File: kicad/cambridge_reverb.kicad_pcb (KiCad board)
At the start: 2 copper layers, 190 x 115 mm, 144 parts, among them IC1 TL072CP, IC2 TL072CP, Q1 MMBF5457, Q2 MMBF5457, T1 reuse / AnTek AS-0524, U1 LM317T

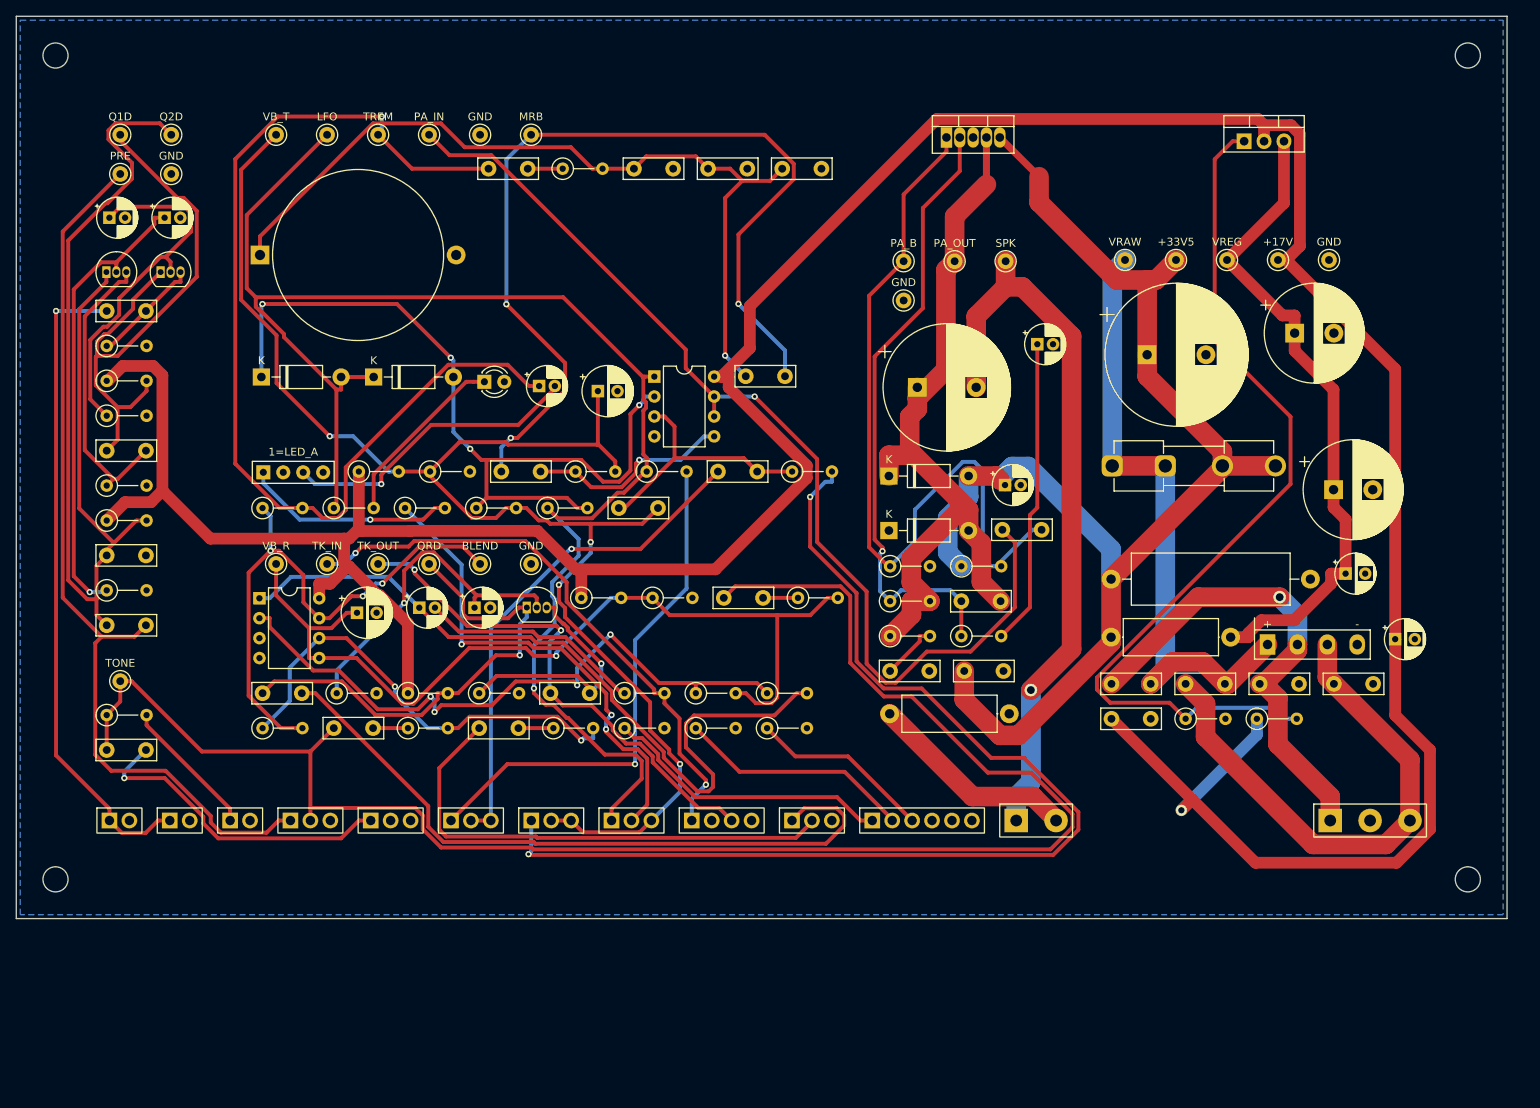
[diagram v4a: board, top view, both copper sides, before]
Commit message: Tone stack: Bass + Treble (passive James) with a switchable mid cut (errata #20)
The panel has Bass and Treble pots, but the design carried a single treble-cut
"Tone" substitute -- and the recovered preamp coupling was the 470 pF chime cap
alone, a 1.3 kHz high-pass that passed no bass at all. Replace both:

- C_cpl_out 1 uF full-band coupling from Q2's drain; C_treble 470 pF becomes a
  bright cap across the top of the volume pot.
- Passive James (Thomas-Vox) Bass/Treble network -- the originals' topology,
  asymmetric, more cut than boost, kept over an active Baxandall so the amp
  keeps its character -- driven by a TL074 (IC3: input buffer, x2 make-up,
  gyrator, output buffer) on its own mid-rail VBIAS_3. Both pots 250k lin in
  the original holes.
- MID CUT toggle for honky pickups: R_mid + a switched series-resonant gyrator
  shunt (1.86 H simulated + 22 nF): -9.6 dB at ~800 Hz, Q ~0.6, flat when off,
  no DC across the switch. SW_MID sits in the original line-reverse switch
  hole -- no new panel holes.
- SPICE: ac_tonestack.cir rewritten rail-aware (all IC3 nodes 8.50 V, noon
  -0.21 dB, notch -9.65 dB at 796 Hz); sweep_tonestack.cir sweeps both pots
  and the switch; results committed.

Generator / placer / router:
- OPAMP14 and SW_SPST symbols, VB_3 / TMK test points (28), BOM rows for IC3,
  the DIP-14 socket, POT_BASS/POT_TREB, SW_MID.
- gen_pcb: tighter profiles (THT 1.2 mm gap / 3.5 mm channels, SMD 0.4 mm),
  overflow repair by moving width between columns, small parts kept in
  schematic order on the shelves, tone/preamp column weighted wider, TP cells
  6x4.5 with the courtyard flush to the cell, input-jack pads down the LEFT
  edge on the 155x90 board (the bottom edge is ~9 mm short for 13 groups),
  keepout rule areas (2 mm edge frame + M3 hole squares) exported to the
  router.
- route_board: refuse a board without its .kicad_pro (a copy routed away from
  the project came back with 0.2 mm tracks and 400 DRC errors); prune
  zero-length segments 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
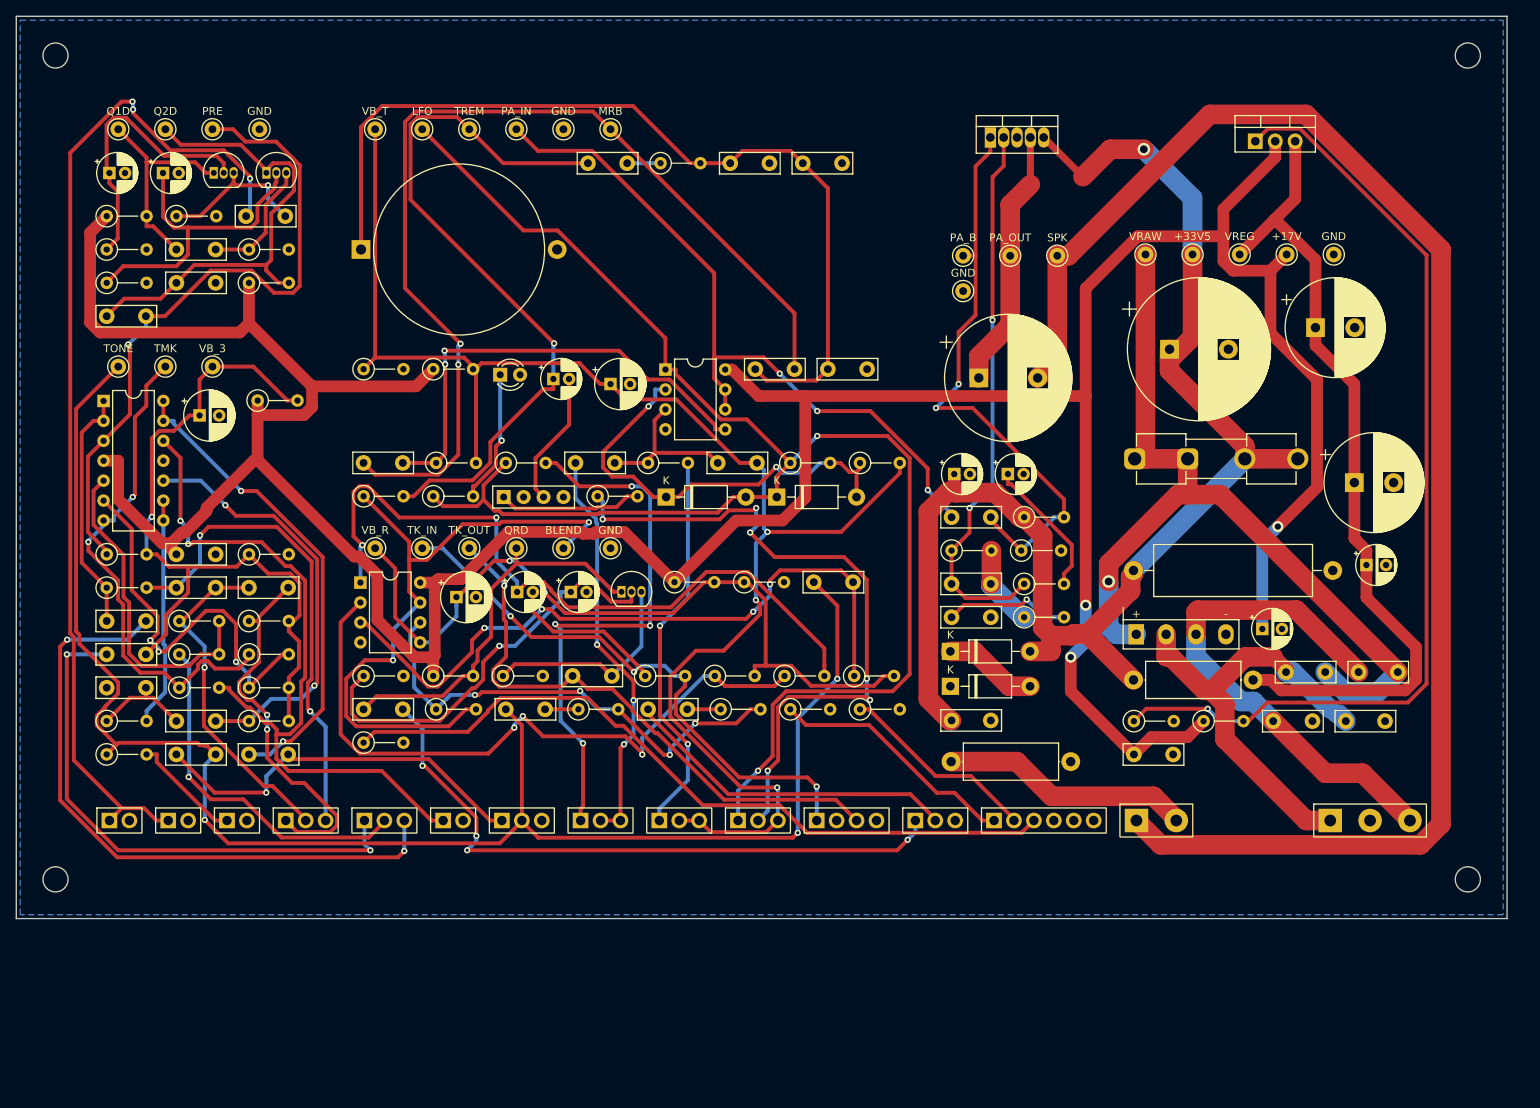
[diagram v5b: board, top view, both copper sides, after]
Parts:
- removed C_cut: 10nF, C_Disc_D7.5mm_W2.5mm_P5.00mm
- removed POT_TONE: 100k lin, WirePad_1x03_P2.54mm_D1.2mm
- added C_byp3: 100nF, C_Disc_D7.5mm_W2.5mm_P5.00mm, F.Cu at (20.4, 68.6)
- added C_cpl_out: 1uF, C_Disc_D7.5mm_W2.5mm_P5.00mm, F.Cu at (11.5, 38.2)
- added C_gg: 1.8nF, C_Disc_D7.5mm_W2.5mm_P5.00mm, F.Cu at (20.4, 89.8)
- added C_j1: 22nF, C_Disc_D7.5mm_W2.5mm_P5.00mm, F.Cu at (20.4, 72.8)
- added C_j2: 22nF, C_Disc_D7.5mm_W2.5mm_P5.00mm, F.Cu at (29.7, 72.8)
- added C_j3: 2.2nF, C_Disc_D7.5mm_W2.5mm_P5.00mm, F.Cu at (11.5, 77.1)
- added C_j4: 2.2nF, C_Disc_D7.5mm_W2.5mm_P5.00mm, F.Cu at (11.5, 81.3)
- added C_res: 22nF, C_Disc_D7.5mm_W2.5mm_P5.00mm, F.Cu at (11.5, 85.6)
- added C_tout: 1uF, C_Disc_D7.5mm_W2.5mm_P5.00mm, F.Cu at (29.7, 94.1)
- added C_vb3: 47uF/25V, CP_Radial_D6.3mm_P2.50mm, F.Cu at (23.4, 50.9)
- added IC3: TL074CN, DIP-14_W7.62mm, F.Cu at (11.1, 49.0)
- added POT_BASS: 250k lin, WirePad_1x03_P2.54mm_D1.2mm, F.Cu at (34.3, 102.5)
- added POT_TREB: 250k lin, WirePad_1x03_P2.54mm_D1.2mm, F.Cu at (44.4, 102.5)
- added R_gL: 4.7k, R_Axial_DIN0207_L6.3mm_D2.5mm_P5.08mm_Vertical, F.Cu at (11.5, 89.8)
- added R_gg: 220k, R_Axial_DIN0207_L6.3mm_D2.5mm_P5.08mm_Vertical, F.Cu at (29.7, 89.8)
- added R_inb: 1M, R_Axial_DIN0207_L6.3mm_D2.5mm_P5.08mm_Vertical, F.Cu at (11.5, 68.6)
- added R_j1: 10k, R_Axial_DIN0207_L6.3mm_D2.5mm_P5.08mm_Vertical, F.Cu at (11.5, 72.8)
- added R_j2: 10k, R_Axial_DIN0207_L6.3mm_D2.5mm_P5.08mm_Vertical, F.Cu at (29.7, 77.1)
- added R_j3: 68k, R_Axial_DIN0207_L6.3mm_D2.5mm_P5.08mm_Vertical, F.Cu at (20.8, 77.1)
- added R_j4: 1k, R_Axial_DIN0207_L6.3mm_D2.5mm_P5.08mm_Vertical, F.Cu at (20.8, 81.3)
- added R_mid: 10k, R_Axial_DIN0207_L6.3mm_D2.5mm_P5.08mm_Vertical, F.Cu at (20.8, 85.6)
- added R_mk1: 10k, R_Axial_DIN0207_L6.3mm_D2.5mm_P5.08mm_Vertical, F.Cu at (29.7, 81.3)
- added R_mk2: 10k, R_Axial_DIN0207_L6.3mm_D2.5mm_P5.08mm_Vertical, F.Cu at (29.7, 85.6)
- added R_vb31: 100k, R_Axial_DIN0207_L6.3mm_D2.5mm_P5.08mm_Vertical, F.Cu at (30.8, 49.0)
- added R_vb32: 100k, R_Axial_DIN0207_L6.3mm_D2.5mm_P5.08mm_Vertical, F.Cu at (29.7, 68.6)
- added SW_MID: MID CUT, WirePad_1x02_P2.54mm_D1.2mm, F.Cu at (54.4, 102.5)
- added TP_MK_OUT: TMK, TestPoint_THT_D2.0mm_Label, F.Cu at (19.0, 44.6)
- added TP_VBIAS_3: VB_3, TestPoint_THT_D2.0mm_Label, F.Cu at (25.0, 44.6)
- moved D_lfo2 53.8 mm to (82.8, 61.3)
- moved D_lfo1 53.6 mm to (96.9, 61.3)
- moved R_fs_mrb 51.5 mm to (44.3, 92.6)
- moved R_lfo_fb2 49.2 mm to (107.5, 56.9)
- moved TP_TONE_OUT 40.1 mm to (13.0, 44.6)
- moved R_s2 39.2 mm to (11.5, 34.0)
- moved C_pres 35.9 mm to (20.4, 34.0)
- moved R_d2 35.3 mm to (29.7, 34.0)
- moved R_g2 35.1 mm to (29.7, 29.7)
- moved R_lfo_fb1 31.5 mm to (98.7, 56.9)
- moved VTL1 30.8 mm to (62.1, 61.3)
- moved C_cpl12 27.1 mm to (20.4, 29.7)
- moved POT_VOL 27.0 mm to (61.9, 102.5)
- moved C_mrb_750 26.2 mm to (103.4, 45.0)
- moved R_led 24.6 mm to (74.1, 61.2)
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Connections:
- C_treble pad 1: Q2D -> VOLTOP
- C_treble pad 2: PREAMP_OUT -> TONE_OUT
- POT_VOL pad 1: PREAMP_OUT -> VOLTOP
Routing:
- net SPK_P: track 93.3 -> 194.6 mm, vias 1 -> 0
- net VBIAS_3: track 0.00 -> 97.5 mm, vias 0 -> 1
- net SPD_B: track 142.7 -> 50.0 mm
- net MID: track 0.00 -> 91.6 mm, vias 0 -> 2
- net DRVP: track 4.45 -> 88.0 mm, vias 0 -> 4
- net JTA: track 0.00 -> 83.0 mm, vias 0 -> 2
- net FS_MRB: track 23.4 -> 95.6 mm
- net Q2D: track 130.8 -> 60.6 mm
- net JTB: track 0.00 -> 69.0 mm, vias 0 -> 2
- net MK_OUT: track 0.00 -> 64.7 mm, vias 0 -> 2
- net JA: track 0.00 -> 62.4 mm, vias 0 -> 2
- net OBUF: track 0.00 -> 61.4 mm, vias 0 -> 2
- net GYP: track 0.00 -> 54.5 mm, vias 0 -> 2
- net MKN: track 0.00 -> 51.3 mm, vias 0 -> 3
- net VOLTOP: track 0.00 -> 50.2 mm, vias 0 -> 1
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
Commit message: Noise, hum, crosstalk and thermal models; three design fixes; JLCPCB rules and cost
New models (docs/06c, spice/): a .noise run of the whole front end including the
LM317's own rail noise, the rail-ripple paths to the speaker, a vactrol-level tremolo
depth model, an electro-thermal LM1875 ladder, and a geometric crosstalk audit of the
routed boards (kicad/gen/crosstalk_audit.py). They found three defects:

- Errata #21 (hum + hiss): the LM1875 bias divider had no bypass (+4 dB ripple to
  speaker, 0.4 Vrms of 100 Hz at idle) and the LM317's 0.5 mV of noise reached the
  0 dB-PSRR JFET stages (23 dB above their floor, SNR 34 dB). Fixed with C_bref +
  R_bias3 on the power amp, C_adj on the regulator, and an RC-decoupled +17V_PRE rail
  for Q1/Q2/Q_rec: hum 408 mV -> 0.3 mV, EIN 37 -> 2.7 uV, SNR 34 -> 57 dB.
- Errata #22 (tremolo depth 1.7 dB): the vactrol LED was returned to ground from a
  mid-rail LFO -> 7 mA DC, a fixed -20 dB pad. LED limiter (2 V swing, LED_rate is one
  limiter LED) + Q_trem 2N3904/MMBT3904 emitter follower AC-coupled from the depth
  pot -> 15 dB depth, 0.8 dB insertion loss.
- Errata #23 (fab): stock TO-92 and the LM1875 footprint were under JLCPCB's 0.18 mm
  annular-ring minimum -> TO-92_Inline_Wide and 1.5 mm LM1875 pads; both .kicad_pro
  carry JLC's 2-layer limits as DRC constraints. Cost: all SMD caps 1206 (basic
  library), "(opt)" MRB caps DNP, gyrator on E24 values (same 1.86 H): 7 -> 2
  extended part types, ~$32 -> ~$17 assembly for five boards (kicad/gen/jlc_cost.py);
  three fiducials on the SMD board.

Crosstalk -> two routing rules (.kicad_dru: HighCurrent 0.6/0.4 mm and TankDrive
1.2/0.8 mm from signal copper, THT/SMD) that route_board.py also hands the router as
class clearances; keepout rule areas along the edge and around the mounting holes.
Thermal: Part 5's <= 2.5 K/W heatsink confirmed with numbers (Tj 97 C at 40 C ambient,
worst-case sine; 8-10 K/W clip-ons reach shutdown).

Placer: short parts stack beside tall ones i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
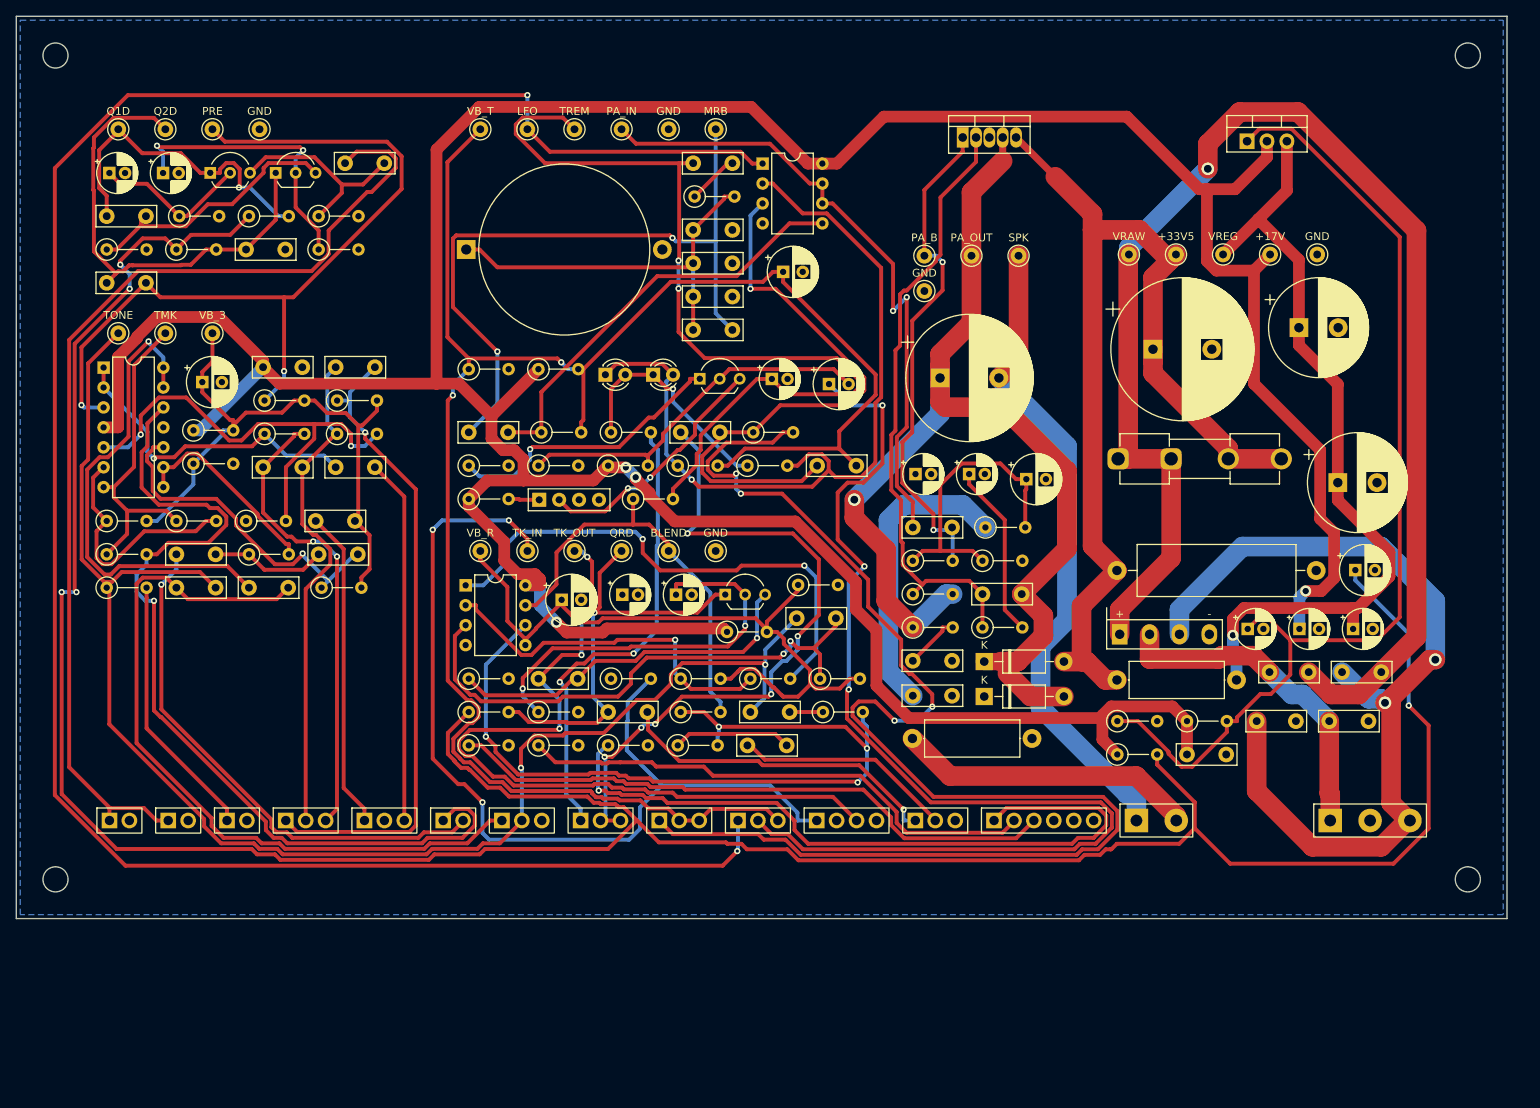
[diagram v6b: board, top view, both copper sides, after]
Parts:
- removed D_lfo1, D_lfo2: 1N4148, D_DO-41_SOD81_P10.16mm_Horizontal
- removed the Q_rec at (77.1, 73.4)
- removed R_led: 1k, R_Axial_DIN0207_L6.3mm_D2.5mm_P5.08mm_Vertical
- removed R_led_diag: 2.2k, R_Axial_DIN0207_L6.3mm_D2.5mm_P5.08mm_Vertical
- added C_adj: 10uF/25V, CP_Radial_D5.0mm_P2.00mm, F.Cu at (156.9, 78.1)
- added C_bref: 100uF/25V, CP_Radial_D6.3mm_P2.50mm, F.Cu at (128.7, 59.0)
- added C_drv: 100uF/25V, CP_Radial_D6.3mm_P2.50mm, F.Cu at (103.6, 46.9)
- added C_pre: 220uF/25V, CP_Radial_D6.3mm_P2.50mm, F.Cu at (170.7, 70.6)
- added LED_lim: 3mm red, LED_D3.0mm, F.Cu at (75.1, 45.7)
- added Q_rec: MMBF5457, TO-92_Inline_Wide, F.Cu at (90.4, 73.7)
- added Q_trem: 2N3904, TO-92_Inline_Wide, F.Cu at (87.1, 46.2)
- added R_b1: 180k, R_Axial_DIN0207_L6.3mm_D2.5mm_P5.08mm_Vertical, F.Cu at (75.4, 57.3)
- added R_b2: 10k, R_Axial_DIN0207_L6.3mm_D2.5mm_P5.08mm_Vertical, F.Cu at (66.5, 57.3)
- added R_bias3: 22k, R_Axial_DIN0207_L6.3mm_D2.5mm_P5.08mm_Vertical, F.Cu at (114.3, 69.4)
- added R_c: 100R, R_Axial_DIN0207_L6.3mm_D2.5mm_P5.08mm_Vertical, F.Cu at (57.7, 61.5)
- added R_e: 470R, R_Axial_DIN0207_L6.3mm_D2.5mm_P5.08mm_Vertical, F.Cu at (57.7, 57.3)
- added R_pre: 100R, R_Axial_DIN0207_L6.3mm_D2.5mm_P5.08mm_Vertical, F.Cu at (140.3, 94.1)
- C_gg: value 1.8nF -> 2.2nF
- Q1, Q2: footprint TO-92_Inline -> TO-92_Inline_Wide
- R_gg: value 220k -> 180k
- moved R_fs_trem 41.2 mm to (66.5, 92.9)
- moved C_j3 35.2 mm to (40.7, 57.5)
- moved R_trem1 34.4 mm to (78.6, 61.5)
- moved C_j4 31.6 mm to (38.2, 64.3)
- moved R_j3 31.2 mm to (40.9, 53.2)
- moved C_drymix 31.2 mm to (93.6, 88.7)
- moved C_rev4 31.2 mm to (75.4, 88.7)
- moved R_drymix 31.2 mm to (102.8, 88.7)
- moved R_mixfb 31.2 mm to (84.7, 88.7)
- moved R_j2 30.3 mm to (40.9, 49.0)
- moved C_j2 30.2 mm to (40.7, 44.7)
- moved IC2 29.0 mm to (95.1, 18.8)
- moved R_inb 28.1 mm to (31.6, 49.0)
- moved R_j1 28.1 mm to (31.6, 53.2)
- moved R_gL 27.9 mm to (29.7, 68.6)
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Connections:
- LED_rate pad 1: DLED -> LFO_OUT
- LED_rate pad 2: GND -> LFO_N
- R_bias1 pad 2: PA_BIAS -> PA_BREF
- R_bias2 pad 1: PA_BIAS -> PA_BREF
- R_d1 pad 1: +17V -> +17V_PRE
- R_d2 pad 1: +17V -> +17V_PRE
- R_rec1 pad 1: +17V -> +17V_PRE
- VTL1 pad 2: GND -> QC
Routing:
- net +17V_PRE: track 0.00 -> 362.8 mm, vias 0 -> 5
- net SPD_B: track 50.0 -> 176.8 mm, vias 2 -> 4
- net SPK_P: track 194.6 -> 83.8 mm
- net LFO_OUT: track 205.4 -> 305.0 mm, vias 2 -> 3
- net PA_OUT: track 55.8 -> 146.5 mm, vias 0 -> 1
- net VRAW: track 110.6 -> 180.5 mm
- net MIDSW: track 0.00 -> 67.4 mm, vias 0 -> 1
- net MRB_T: track 115.4 -> 50.0 mm
- net FS_REV: track 31.8 -> 92.2 mm, vias 0 -> 1
- net DPT_W: track 87.6 -> 142.1 mm, vias 6 -> 3
- net LFO_P: track 20.6 -> 74.9 mm, vias 0 -> 1
- net TANK_IN: track 72.3 -> 123.4 mm
- net AC2: track 65.7 -> 114.2 mm, vias 0 -> 2
- net LFO_N: track 55.3 -> 102.7 mm, vias 2 -> 1
- net QB: track 0.00 -> 47.4 mm
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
